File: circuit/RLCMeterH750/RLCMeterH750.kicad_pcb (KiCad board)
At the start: 2 copper layers, 80 x 65 mm, 141 parts, among them J1 SWD, J2 USB_B_Micro, J3 ILI_9321(2.2inch), J4 DUT, SW1 EVQWKL001, SW2 PowerOn, U1 STM32H750VITx, U10 AD8031, U11 AD8031, U12 AD9833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

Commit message: - вроде все провода соединили
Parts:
- added C59: 100n, Capacitor_SMD:C_0603_1608Metric, F.Cu at (118.0, 139.5)
- moved R21 13.4 mm to (122.1, 124.6)
- moved C26 12.3 mm to (122.9, 128.5), turned to 90 degrees
- moved C25 5.33 mm to (122.1, 126.2)
- moved U11 4.94 mm to (126.1, 128.3), turned to 270 degrees
- moved R36 4.70 mm to (126.8, 122.2)
- moved U14 4.02 mm to (131.8, 123.1)
- moved C31 3.95 mm to (123.0, 134.1), turned to 90 degrees
- moved C39 3.69 mm to (133.9, 128.1), turned to 90 degrees
- moved C38 3.49 mm to (129.6, 128.2), turned to 90 degrees
- moved C42 3.26 mm to (137.6, 117.8)
- moved C30 3.10 mm to (123.0, 137.3), turned to 270 degrees
- moved R38 2.87 mm to (121.9, 120.9)
- moved R33 2.83 mm to (132.7, 139.9)
- moved R34 2.79 mm to (131.9, 137.4)
- moved R35 2.44 mm to (128.7, 140.4)
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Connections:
- SW2 pad GND: (no net) -> GND
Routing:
- net +1V5: track 17.1 -> 82.4 mm, vias 0 -> 7
- net S1: track 0.00 -> 63.9 mm, vias 0 -> 2
- net S2: track 0.00 -> 60.4 mm, vias 0 -> 2
- net -2V5: track 92.7 -> 153.0 mm, vias 4 -> 8
- net +3.3VA: track 39.2 -> 93.7 mm, vias 2 -> 7
- net +5V: track 76.2 -> 123.7 mm, vias 5 -> 9
- net Net-(J4-Pad4): track 0.00 -> 35.7 mm
- net Net-(J4-Pad2): track 0.00 -> 18.0 mm
- net Net-(J4-Pad3): track 0.00 -> 17.5 mm
- net GND: track 211.9 -> 228.7 mm, vias 45 -> 119
- net Net-(R45-Pad1): track 0.00 -> 13.5 mm
- net Net-(U11-Pad1): track 0.00 -> 13.0 mm, vias 0 -> 2
- net Net-(R35-Pad1): track 0.00 -> 10.4 mm
- net Net-(C31-Pad1): track 0.00 -> 9.85 mm, vias 0 -> 2
- net Net-(C30-Pad1): track 0.00 -> 9.53 mm, vias 0 -> 2
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
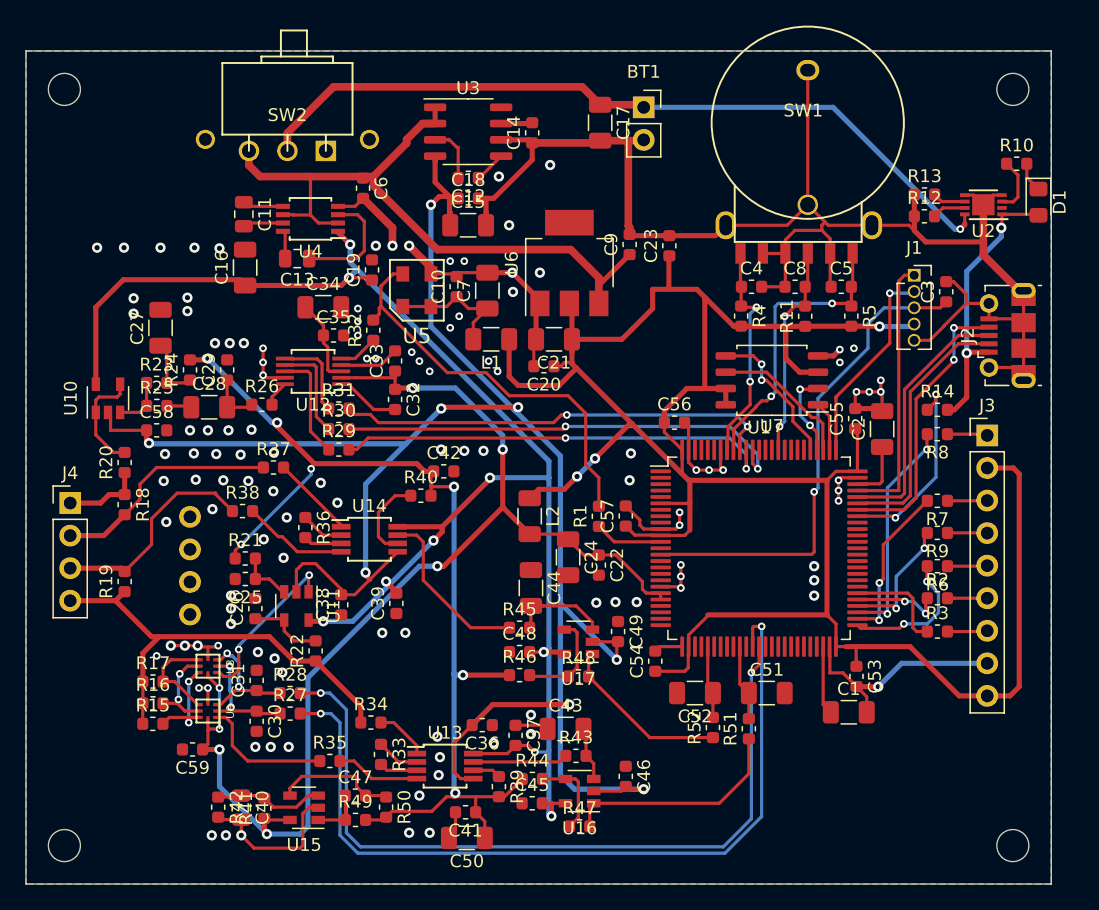
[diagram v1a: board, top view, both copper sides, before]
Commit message: - расставляли номера деталей, чтобы их было видно на плате
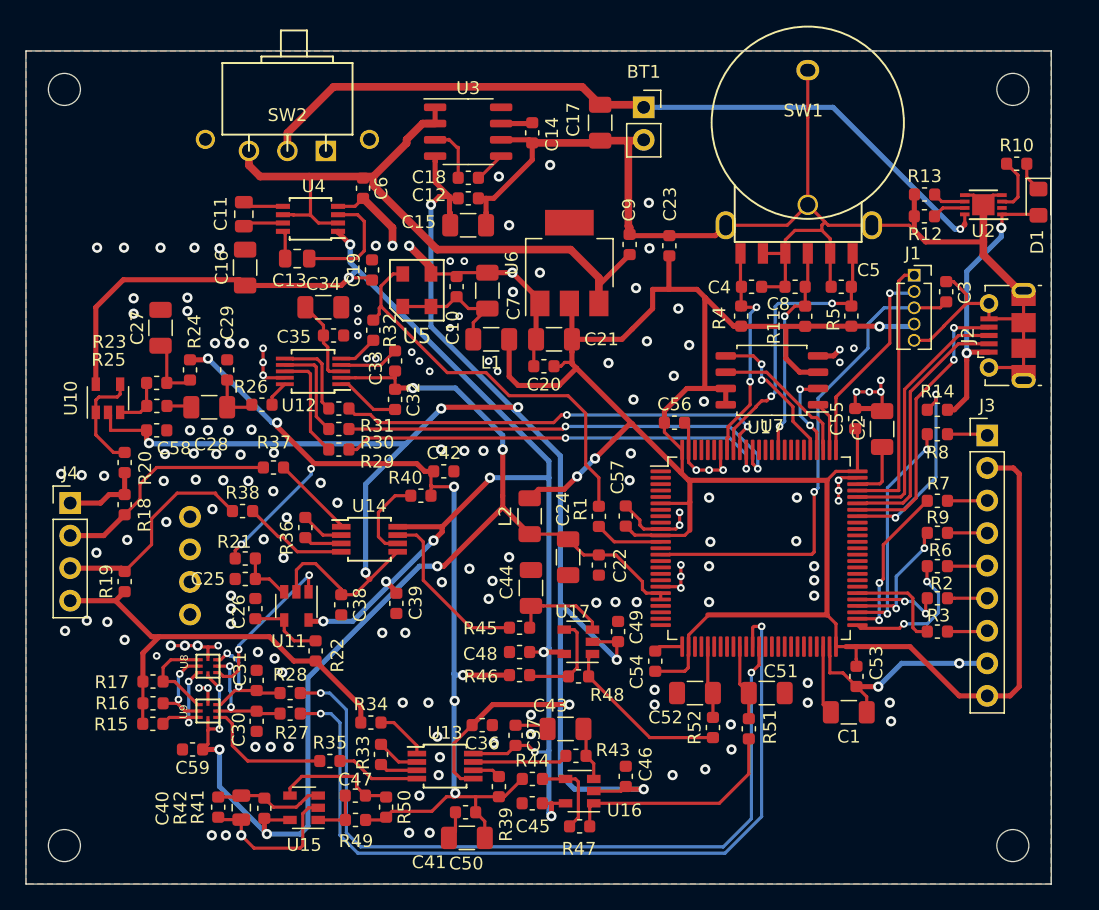
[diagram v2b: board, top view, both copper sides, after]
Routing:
- net GND: vias 119 -> 162
- net +1V5: vias 7 -> 8
